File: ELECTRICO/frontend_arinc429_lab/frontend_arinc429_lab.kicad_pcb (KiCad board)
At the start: 2 copper layers, 113 x 71 mm, 34 parts, among them J1 Pico logic I/O, J2 LINE_A/LINE_B/GND, J3 +3V3/+6/-6/GND, U1 TL072/TL082/dual op-amp, U2 MCP6562/LM393 dual comp

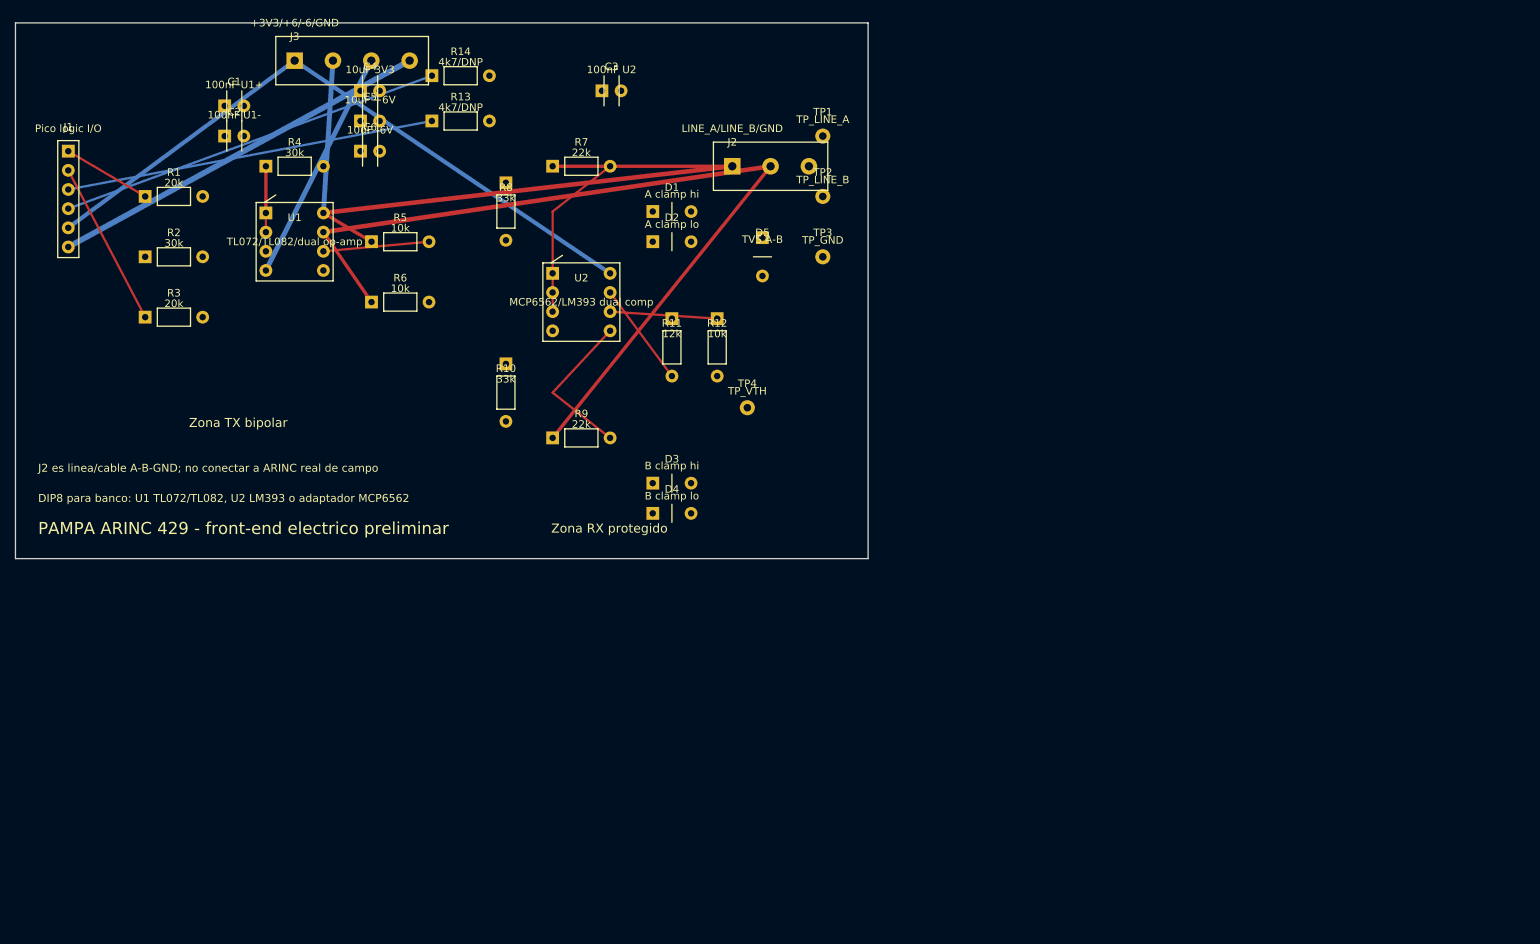
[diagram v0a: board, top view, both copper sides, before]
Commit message: Actualiza frontend electrico y relevamiento de componentes
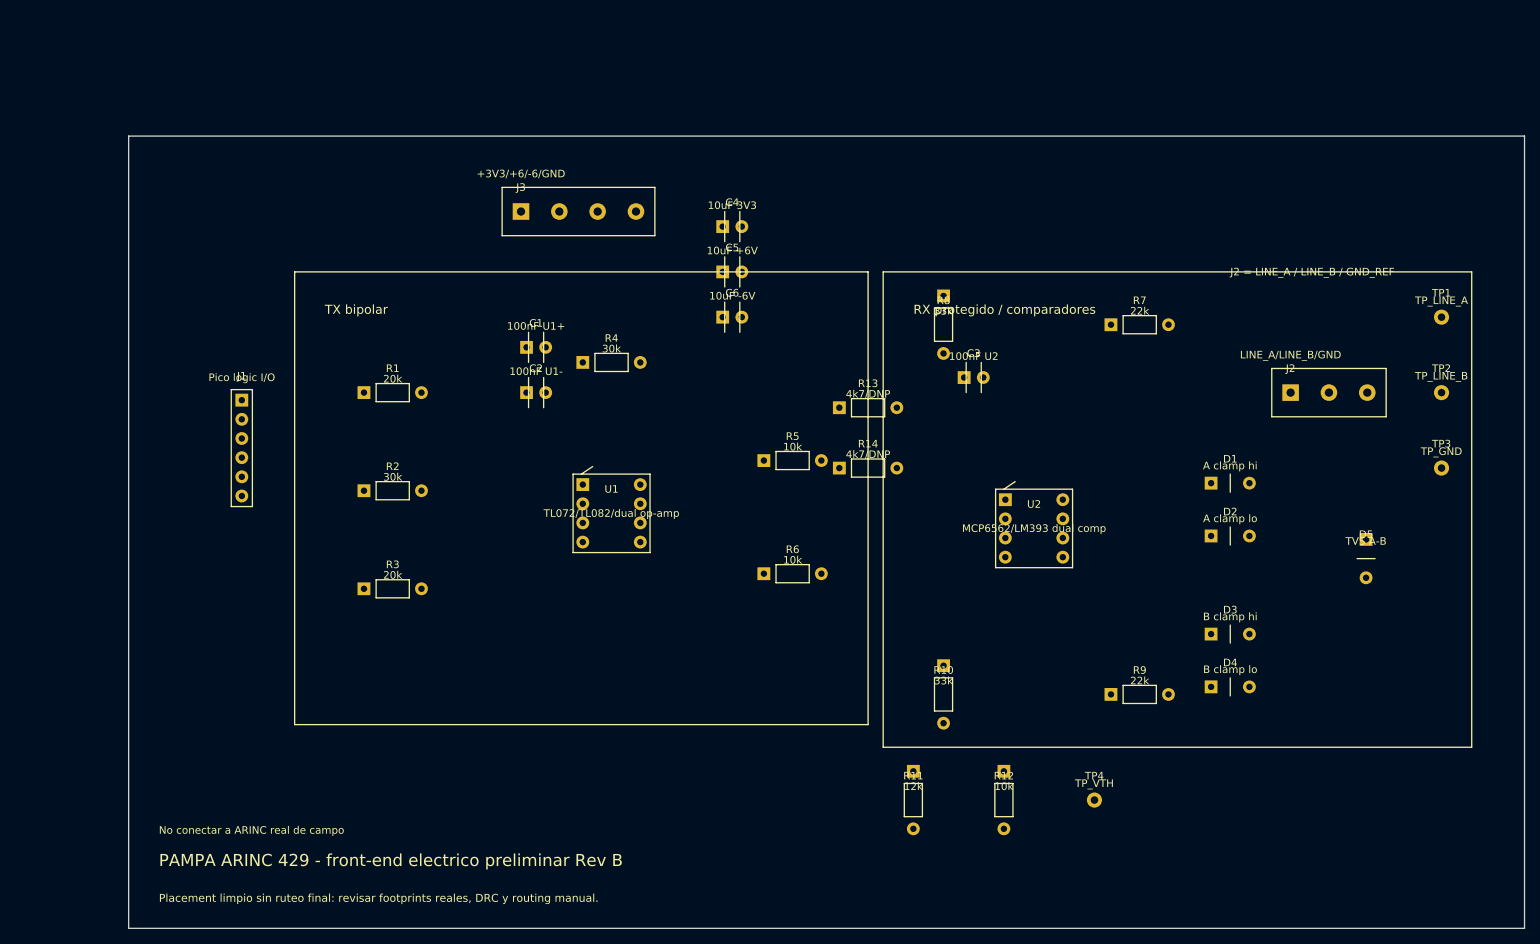
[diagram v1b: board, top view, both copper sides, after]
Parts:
- moved D5 89.4 mm to (184.0, 76.0)
- moved TP3 86.6 mm to (194.0, 64.0)
- moved TP2 86.0 mm to (194.0, 54.0)
- moved TP1 85.4 mm to (194.0, 44.0)
- moved D2 83.6 mm to (166.0, 73.0)
- moved D1 82.3 mm to (166.0, 66.0)
- moved R9 81.4 mm to (154.0, 94.0)
- moved J2 79.8 mm to (174.0, 54.0)
- moved D4 77.5 mm to (166.0, 93.0)
- moved R7 76.9 mm to (154.0, 45.0)
- moved D3 76.7 mm to (166.0, 86.0)
- moved R14 75.0 mm to (118.0, 64.0)
- moved R12 71.0 mm to (136.0, 108.0)
- moved R10 70.5 mm to (128.0, 94.0)
- moved TP4 69.4 mm to (148.0, 108.0)
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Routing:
- net LINE_B: track 117.3 -> 0.00 mm
- net LINE_A: track 92.0 -> 0.00 mm
- net +3V3_LOGIC: track 87.7 -> 0.00 mm
- net GND_COMUN: track 51.5 -> 0.00 mm
- net RX_B_LOGIC: track 51.3 -> 0.00 mm
- net RX_A_LOGIC: track 49.0 -> 0.00 mm
- net -6V_TX: track 31.1 -> 0.00 mm
- net VTH_COMP: track 28.0 -> 0.00 mm
- net A_SENSE: track 23.0 -> 0.00 mm
- net TX_B_LOGIC: track 22.0 -> 0.00 mm
- net B_SENSE: track 20.9 -> 0.00 mm
- net +6V_TX: track 20.2 -> 0.00 mm
- net U1B_NEG: track 14.1 -> 0.00 mm
- net TX_A_LOGIC: track 11.8 -> 0.00 mm
- net U1A_NEG: track 8.73 -> 0.00 mm
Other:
- board size 113 x 71 mm -> 185 x 105 mm
- board text added: "J2 = LINE_A / LINE_B / GND_REF"
- board text added: "No conectar a ARINC real de campo"
- board text added: "PAMPA ARINC 429 - front-end electrico preliminar Rev B"
- board text added: "Placement limpio sin ruteo final: revisar footprints reales, DRC y routing manual."
- board text added: "RX protegido / comparadores"
- board text added: "TX bipolar"
- board text removed: "DIP8 para banco: U1 TL072/TL082, U2 LM393 o adaptador MCP6562"
- board text removed: "J2 es linea/cable A-B-GND; no conectar a ARINC real de campo"
- board text removed: "PAMPA ARINC 429 - front-end electrico preliminar"
- board text removed: "Zona RX protegido"
- board text removed: "Zona TX bipolar"
